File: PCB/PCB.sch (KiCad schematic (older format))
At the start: 19 parts, among them P1 back +5V, T1 BC548C-NPN-TO92-EBC, U1 LCD_HD44870, U2 HALL, U3 DS1820

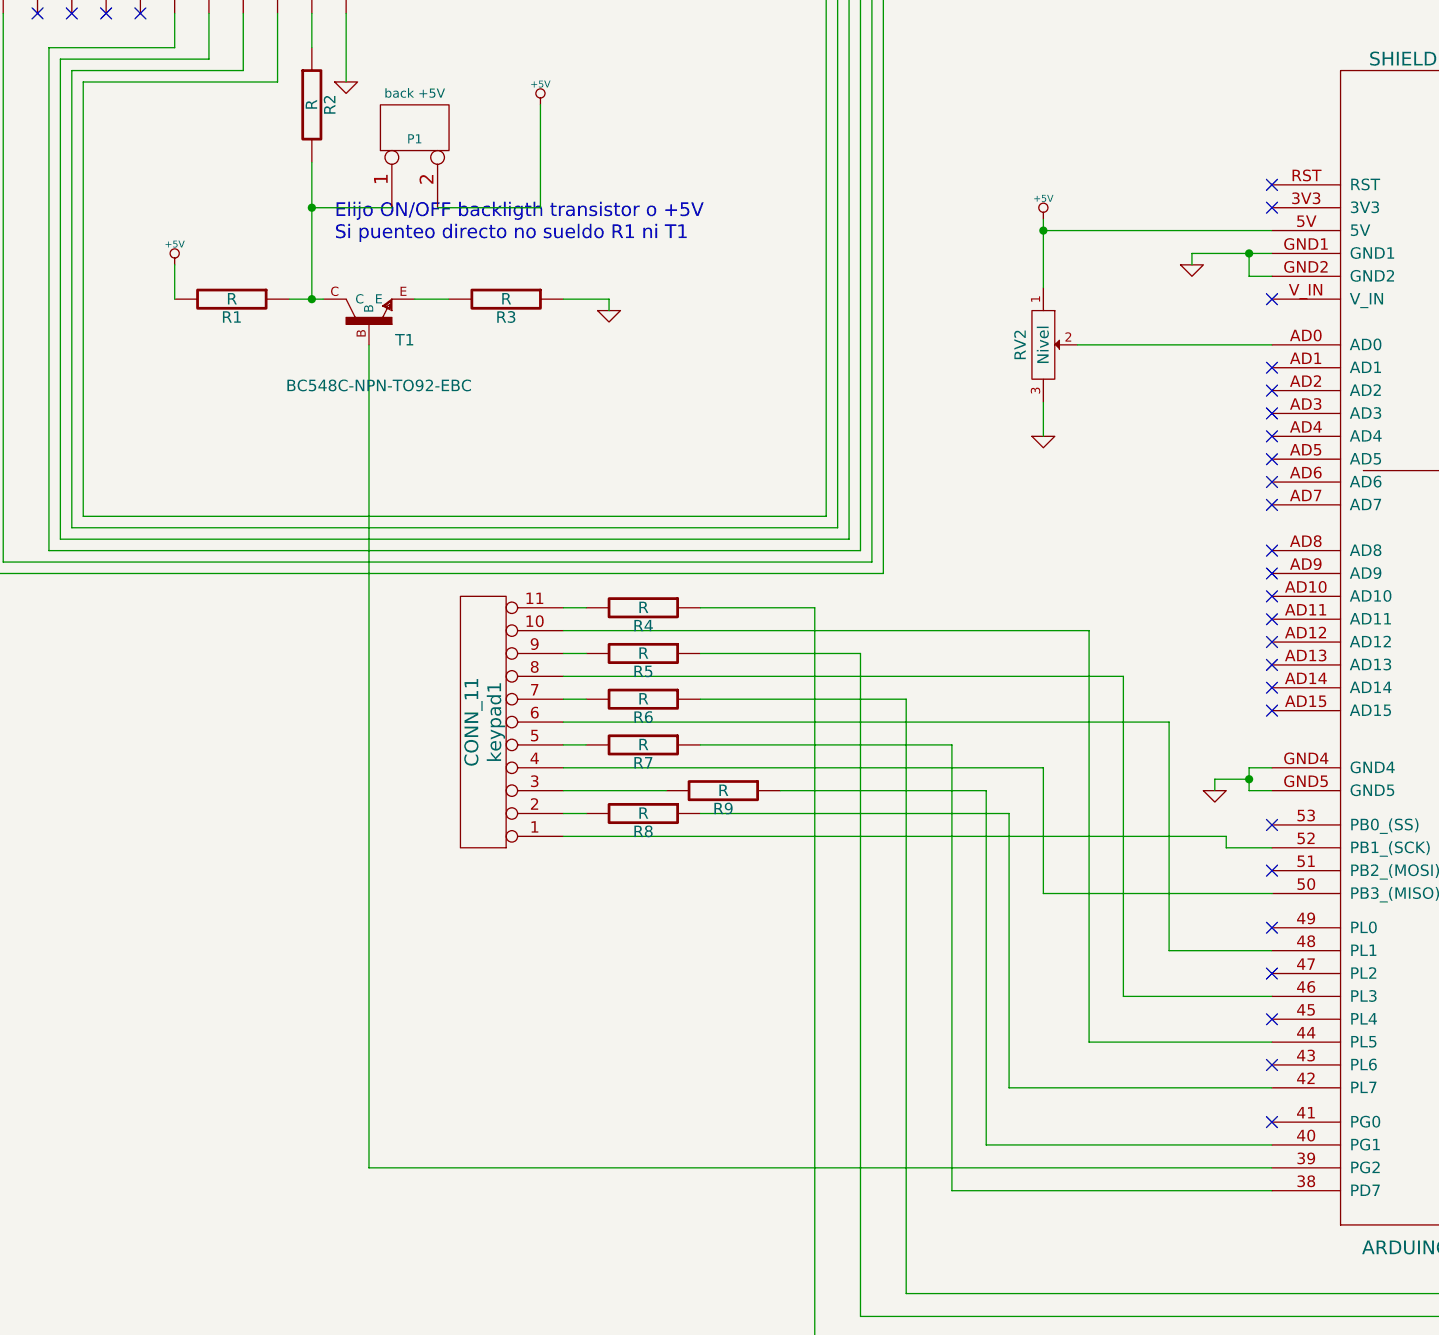
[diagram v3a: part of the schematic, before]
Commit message: PCB (Rev: 2)  + nota PINES.txt para cambiar pines en la próxima
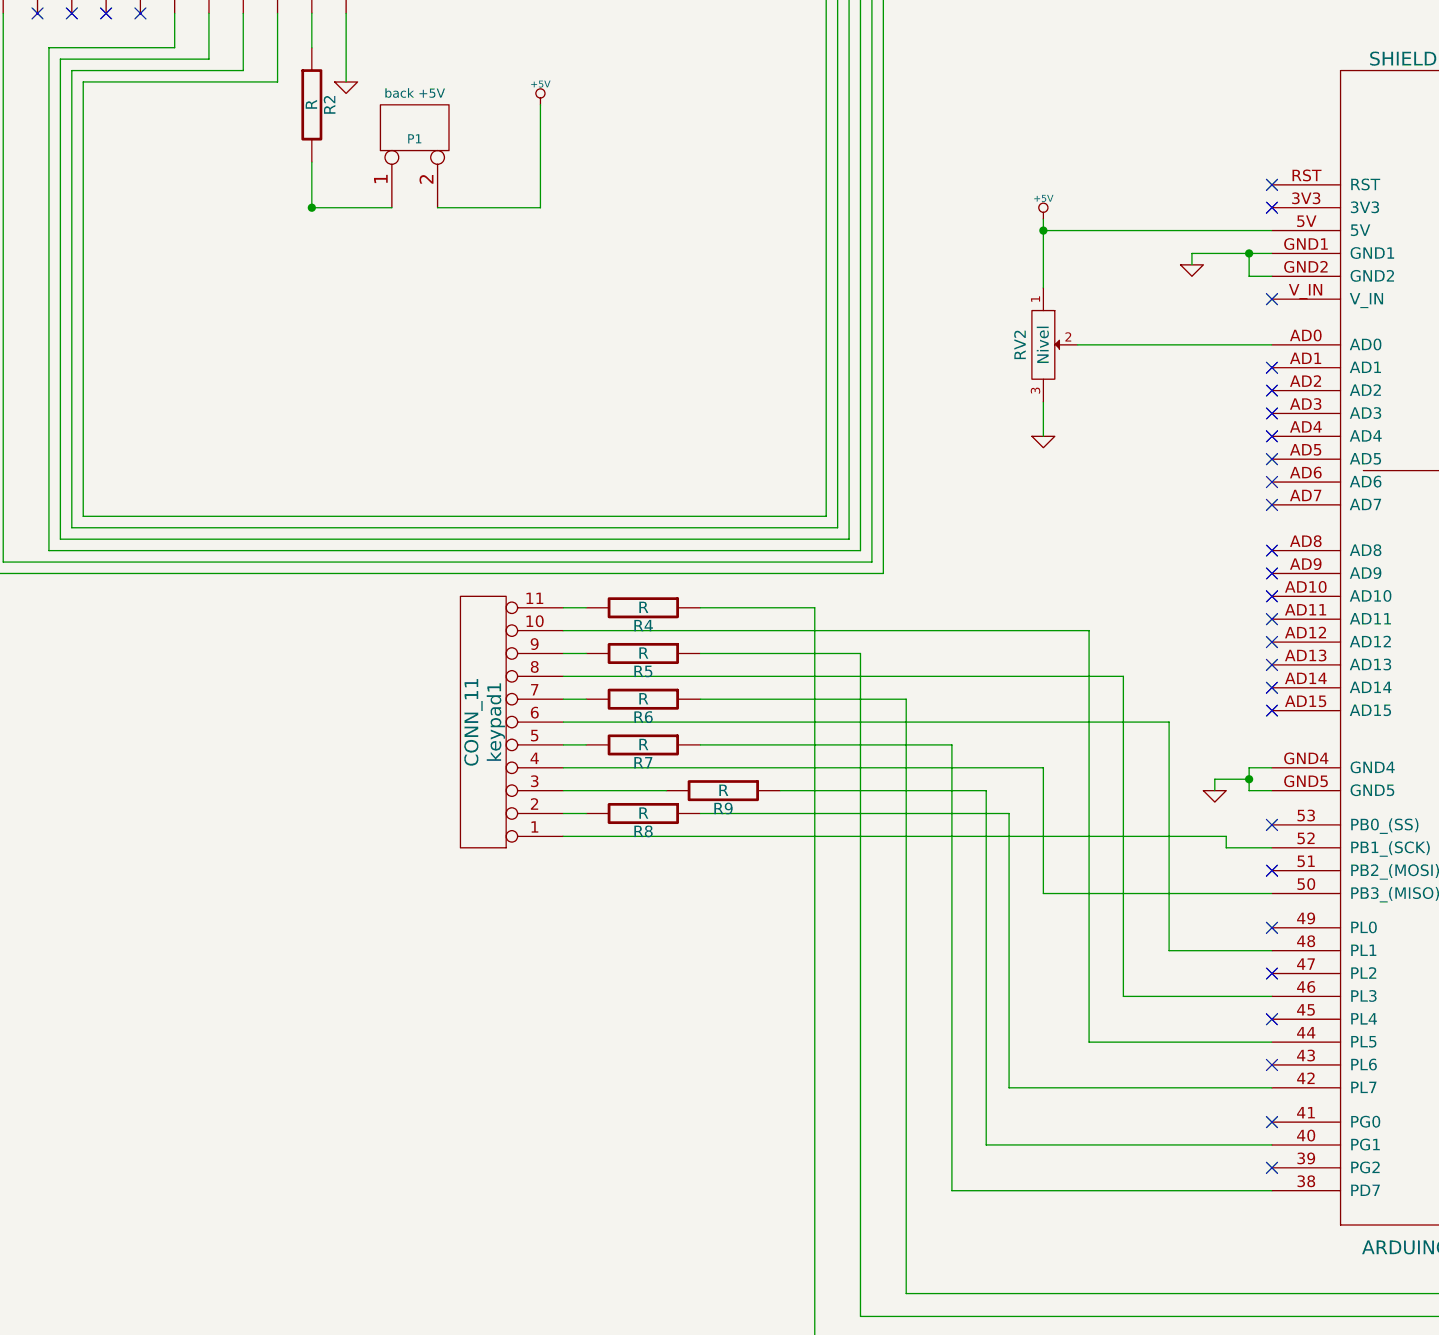
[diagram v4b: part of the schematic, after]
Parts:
- removed R1, R3: R, symbol R
- removed T1: BC548C-NPN-TO92-EBC, transistor-TO92-EBC, symbol BC548C-NPN-TO92-EBC
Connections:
- no-connect marks 58 -> 59
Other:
- note removed: "Elijo ON/OFF backligth transistor o +5V\nSi puenteo directo no sueldo R1 ni T1"
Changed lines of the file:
@@
-EESchema Schematic File Version 2  date mié 25 may 2011 12:11:15 ART
+EESchema Schematic File Version 2  date mié 25 may 2011 16:38:06 ART
 LIBS:power
 LIBS:device
@@
 Comment4 ""
 $EndDescr
+NoConn ~ 9150 7800
+Connection ~ 4950 3600
+Wire Wire Line
+	5300 3600 4950 3600
+Wire Wire Line
+	4950 3600 4950 3400
 Connection ~ 9050 6100
 Wire Wire Line
@@
 	12800 4950 12800 4700
 Wire Wire Line
-	5200 4200 5200 7800
-Wire Wire Line
-	5200 7800 9150 7800
-Wire Wire Line
 	11050 5850 11500 5850
-Connection ~ 4950 3600
-Wire Wire Line
-	5300 3600 4950 3600
 Wire Notes Line
 	11000 4750 11100 4750
@@
 	11100 4550 11000 4550
 Wire Wire Line
-	9050 3800 9050 3900
+	9050 3900 9050 3800
 Wire Wire Line
 	9050 3900 9150 3900
@@
 Wire Wire Line
 	13050 3900 13050 4000
-Wire Wire Line
-	5400 4000 5550 4000
-Wire Wire Line
-	4350 4000 4350 3850
 Wire Wire Line
 	11050 7150 12050 7150
@@
 	4950 2900 4950 2750
 Wire Wire Line
-	5000 4000 4850 4000
-Connection ~ 4950 4000
-Wire Wire Line
-	6050 4000 6250 4000
-Wire Wire Line
-	6250 4000 6250 4050
-Wire Wire Line
 	12900 3700 12900 4000
 Wire Wire Line
@@
 	12650 4400 12650 4450
 Wire Wire Line
-	8800 3850 8800 3800
-Wire Wire Line
-	8800 3800 9150 3800
+	8800 3800 8800 3850
+Wire Wire Line
+	9150 3800 8800 3800
 Connection ~ 9050 3800
 Wire Wire Line
@@
 Wire Wire Line
 	11150 3200 11050 3200
-Wire Wire Line
-	4950 3400 4950 4000
 Wire Wire Line
 	5500 3600 5950 3600
@@
 F 1 "back +5V" V 5550 3250 40  0000 C CNN
 	1    5400 3250
-	0    -1   -1   0
-$EndComp
-$Comp
-L BC548C-NPN-TO92-EBC T1
-U 1 1 4DD6BA68
-P 5200 4100
-F 0 "T1" V 5150 3900 50  0000 L BNN
-F 1 "BC548C-NPN-TO92-EBC" V 4950 3650 50  0000 L BNN
-F 2 "transistor-TO92-EBC" H 5200 4250 50  0001 C CNN
-	1    5200 4100
 	0    -1   -1   0
 $EndComp
@@
 	1    0    0    -1
 $EndComp
-Text Notes 5050 3750 0    60   ~ 0
-Elijo ON/OFF backligth transistor o +5V\nSi puenteo directo no sueldo R1 ni T1
-$Comp
-L GND #PWR010
-U 1 1 4DD6BB76
-P 6250 4050
-F 0 "#PWR010" H 6250 4050 30  0001 C CNN
-F 1 "GND" H 6250 3980 30  0001 C CNN
-	1    6250 4050
-	1    0    0    -1
-$EndComp
-$Comp
-L R R3
-U 1 1 4DD6BB32
-P 5800 4000
-F 0 "R3" V 5880 4000 50  0000 C CNN
-F 1 "R" V 5800 4000 50  0000 C CNN
-	1    5800 4000
-	0    1    1    0
-$EndComp
-$Comp
-L R R1
-U 1 1 4DD6BB29
-P 4600 4000
-F 0 "R1" V 4680 4000 50  0000 C CNN
-F 1 "R" V 4600 4000 50  0000 C CNN
-	1    4600 4000
-	0    1    1    0
-$EndComp
-$Comp
-L +5V #PWR011
-U 1 1 4DD6B81D
-P 4350 3850
-F 0 "#PWR011" H 4350 3940 20  0001 C CNN
-F 1 "+5V" H 4350 3940 30  0000 C CNN
-	1    4350 3850
-	1    0    0    -1
-$EndComp
 $Comp
 L R R2
@@
 $EndComp
 $Comp
-L GND #PWR012
+L GND #PWR010
 U 1 1 4DD6B3E9
 P 5100 3050
-F 0 "#PWR012" H 5100 3050 30  0001 C CNN
+F 0 "#PWR010" H 5100 3050 30  0001 C CNN
 F 1 "GND" H 5100 2980 30  0001 C CNN
 	1    5100 3050
@@
 $EndComp
 $Comp
-L GND #PWR013
+L GND #PWR011
 U 1 1 4DD6B325
 P 2250 3700
-F 0 "#PWR013" H 2250 3700 30  0001 C CNN
+F 0 "#PWR011" H 2250 3700 30  0001 C CNN
 F 1 "GND" H 2250 3630 30  0001 C CNN
 	1    2250 3700
@@
 $EndComp
 $Comp
-L +5V #PWR014
+L +5V #PWR012
 U 1 1 4DD5E415
 P 2250 2500
-F 0 "#PWR014" H 2250 2590 20  0001 C CNN
+F 0 "#PWR012" H 2250 2590 20  0001 C CNN
 F 1 "+5V" H 2250 2590 30  0000 C CNN
 	1    2250 2500
@@
 $EndComp
 $Comp
-L GND #PWR015
+L GND #PWR013
 U 1 1 4DD5E3F1
 P 2850 2950
-F 0 "#PWR015" H 2850 2950 30  0001 C CNN
+F 0 "#PWR013" H 2850 2950 30  0001 C CNN
 F 1 "GND" H 2850 2880 30  0001 C CNN
 	1    2850 2950
@@
 +5V viene de la placa con el micro (usb o conector). \nEsta placa no se alimenta, se cuelga de la otra.
 $Comp
-L +5V #PWR016
+L +5V #PWR014
 U 1 1 4DD5E2E6
 P 8150 3650
-F 0 "#PWR016" H 8150 3740 20  0001 C CNN
+F 0 "#PWR014" H 8150 3740 20  0001 C CNN
 F 1 "+5V" H 8150 3740 30  0000 C CNN
 	1    8150 3650
@@
 $EndComp
 $Comp
-L GND #PWR017
+L GND #PWR015
 U 1 1 4DD5E2A9
 P 8150 4600
-F 0 "#PWR017" H 8150 4600 30  0001 C CNN
+F 0 "#PWR015" H 8150 4600 30  0001 C CNN
 F 1 "GND" H 8150 4530 30  0001 C CNN
 	1    8150 4600

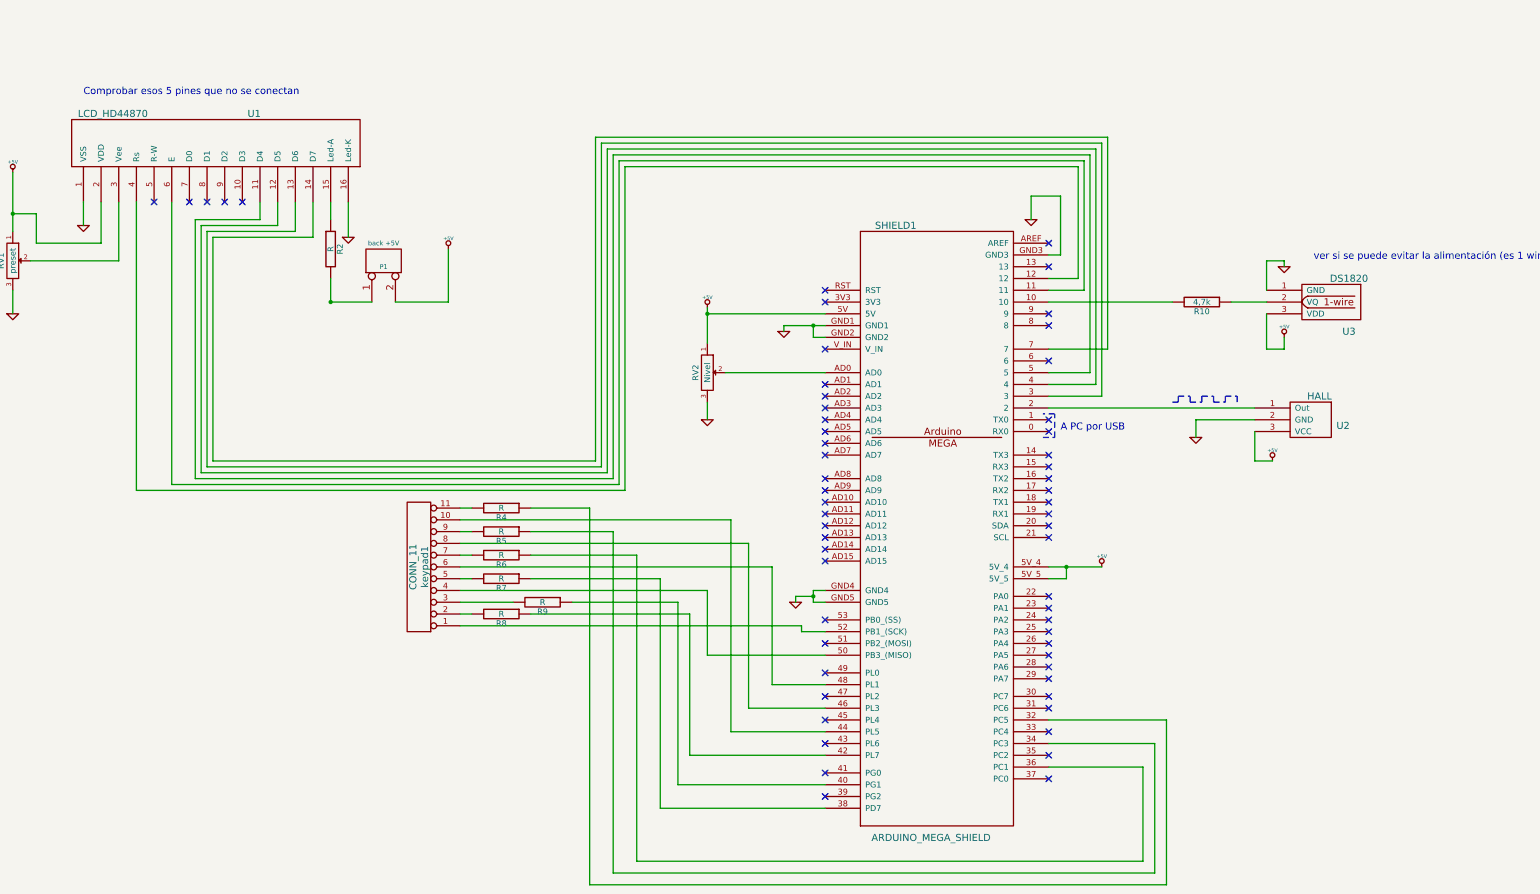
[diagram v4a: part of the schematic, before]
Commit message: PCB completo con Keypad actualizado + 3 leds con sus resistencias
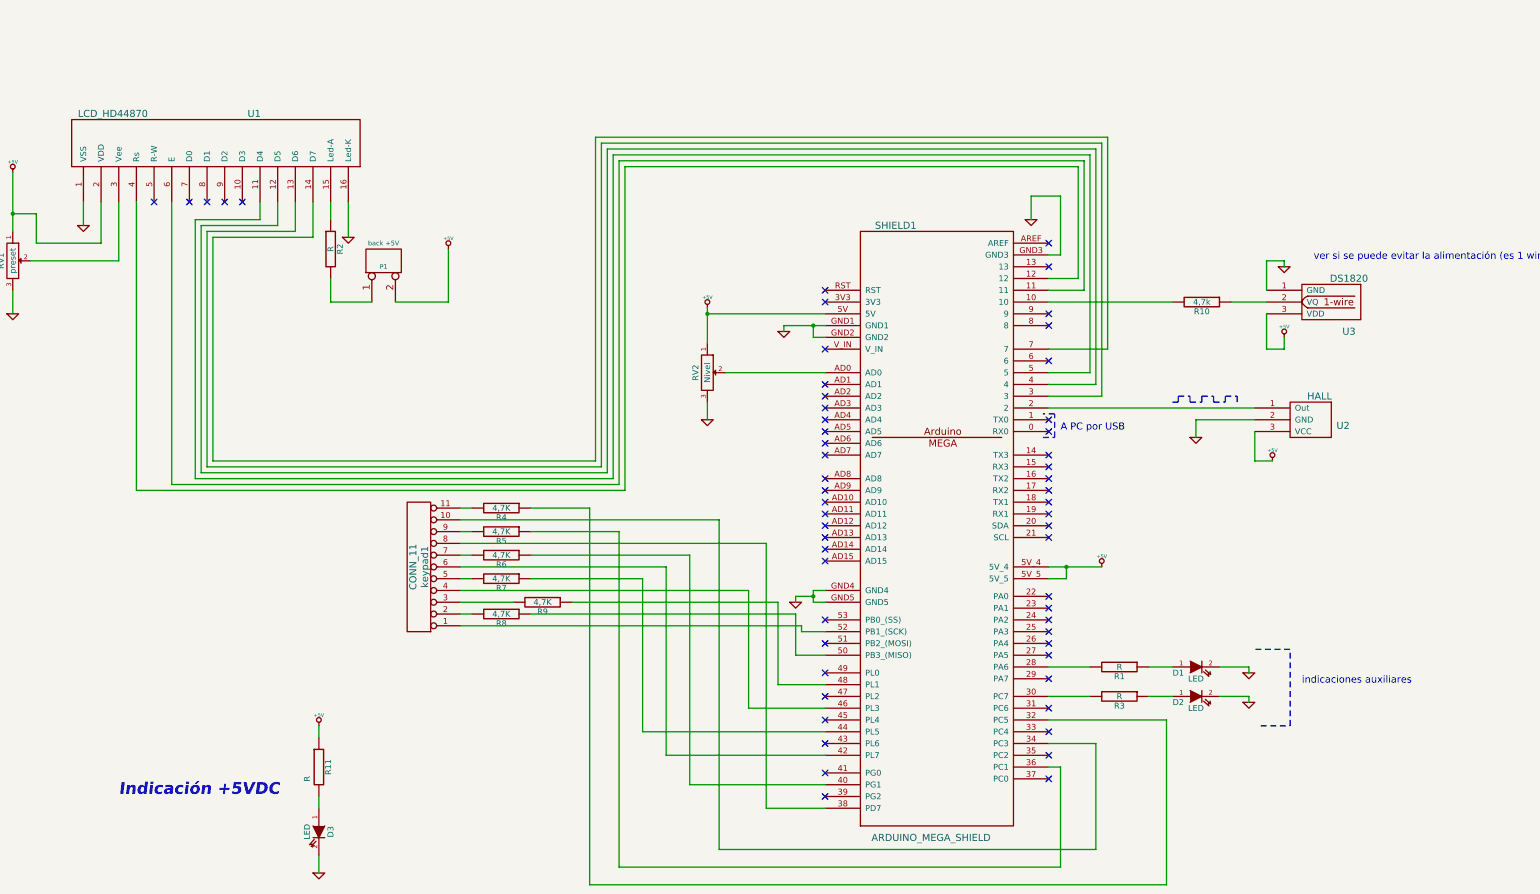
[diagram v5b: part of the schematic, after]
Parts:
- added D1, D2, D3: LED, symbol LED
- added R1, R11, R3: R, symbol R
- R4, R5, R6, R7, R8, R9: value R -> 4,7K
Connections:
- net +5V: now also R11.1
- net GND: now also D1.2 (K), D2.2 (K), D3.2 (K)
- net at SHIELD1.28 (PA6): now also R1.2
- net at SHIELD1.30 (PC7): now also R3.2
- net at SHIELD1.34 (PC3): now also keypad1.10 (P10); no longer R5.1
- net at SHIELD1.36 (PC1): now also R5.1; no longer R6.1
- net at SHIELD1.38 (PD7): now also keypad1.8 (P8); no longer R7.1
- net at SHIELD1.40 (PG1): now also R6.1; no longer R9.1
- net at SHIELD1.42 (PL7): now also keypad1.6 (P6); no longer R8.1
- net at SHIELD1.44 (PL5): now also R7.1; no longer keypad1.10 (P10)
- net at SHIELD1.46 (PL3): now also keypad1.4 (P4); no longer keypad1.8 (P8)
- net at SHIELD1.48 (PL1): now also R9.1; no longer keypad1.6 (P6)
- net at SHIELD1.50 (PB3_(MISO)): now also R8.1; no longer keypad1.4 (P4)
- new net: D1.1 (A), R1.1
- new net: D2.1 (A), R3.1
- new net: D3.1 (A), R11.2
- no-connect marks 59 -> 57
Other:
- note added: "Indicación +5VDC"
- note added: "indicaciones auxiliares"
- note removed: "Comprobar esos 5 pines que no se conectan"
